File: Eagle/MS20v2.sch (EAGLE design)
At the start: 62 parts, among them IC1 LM13700M, IC2 TL074D, T1 2N3906, T2 2N3906

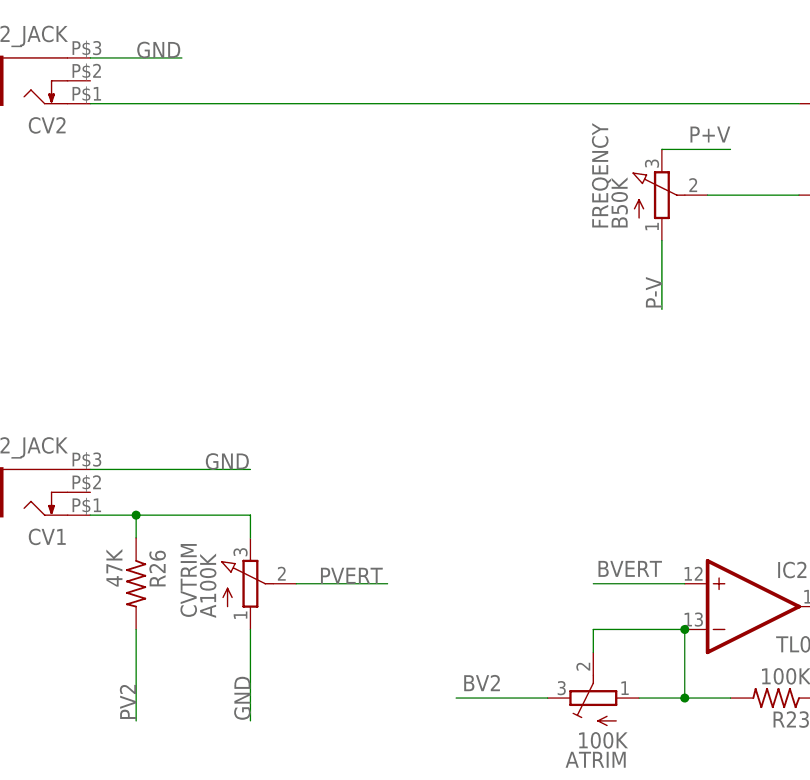
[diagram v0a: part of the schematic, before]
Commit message: updated Pot designations/values
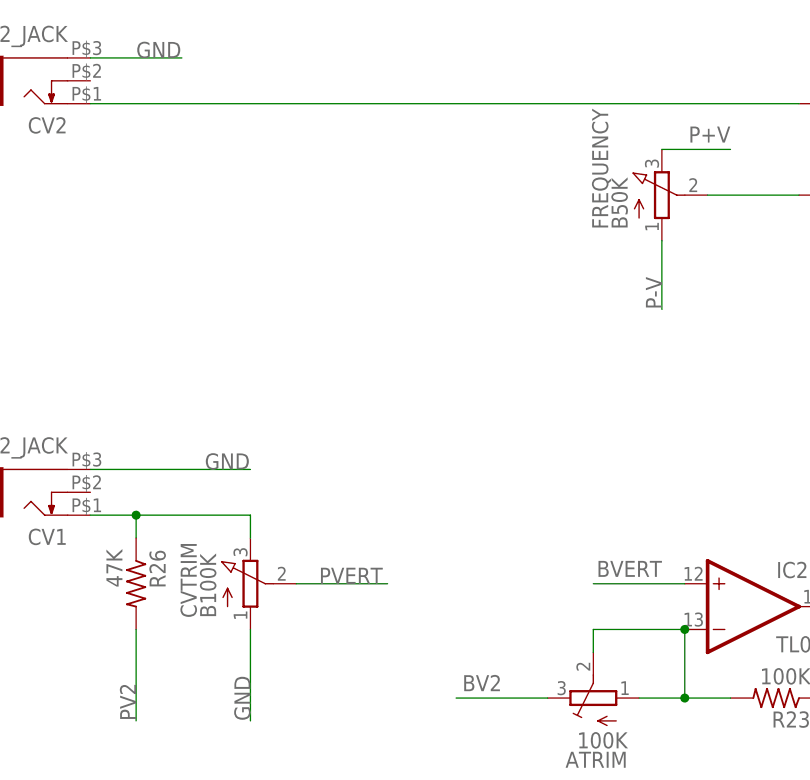
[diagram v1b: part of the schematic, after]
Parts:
- CVTRIM: value A100K -> B100K
- renumbered FREQENCY to FREQUENCY
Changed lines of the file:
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@@
 <part name="ATRIM" library="adafruit" deviceset="TRIMPOT" device="TC33X" value="100K"/>
 <part name="FTUNE" library="adafruit" deviceset="TRIMPOT" device="TC33X" value="1K"/>
-<part name="FREQENCY" library="pot" deviceset="EVU" device="A" technology="F2" value="B50K"/>
-<part name="CVTRIM" library="pot" deviceset="EVU" device="A" technology="F2" value="A100K"/>
+<part name="FREQUENCY" library="pot" deviceset="EVU" device="A" technology="F2" value="B50K"/>
+<part name="CVTRIM" library="pot" deviceset="EVU" device="A" technology="F2" value="B100K"/>
 <part name="INVOL" library="pot" deviceset="EVU" device="A" technology="F2" value="A100K"/>
 <part name="RESONANCE" library="pot" deviceset="EVU" device="A" technology="F2" value="A100K"/>
@@
 <attribute name="VALUE" x="57.15" y="135.89" size="1.778" layer="96" rot="R90"/>
 </instance>
-<instance part="FREQENCY" gate="G$1" x="-2.54" y="205.74" smashed="yes" grouprefs="4">
+<instance part="FREQUENCY" gate="G$1" x="-2.54" y="205.74" smashed="yes" grouprefs="4">
 <attribute name="NAME" x="-8.509" y="201.93" size="1.778" layer="95" rot="R90"/>
 <attribute name="VALUE" x="-6.35" y="201.93" size="1.778" layer="96" rot="R90"/>
@@
 <wire x1="58.42" y1="12.7" x2="63.5" y2="12.7" width="0.1524" layer="91"/>
 <pinref part="C4" gate="G$1" pin="1"/>
-<wire x1="63.5" y1="12.7" x2="63.5" y2="40.64" width="0.1524" layer="91" grouprefs="1"/>
+<wire x1="63.5" y1="12.7" x2="63.5" y2="40.64" width="0.1524" layer="91"/>
 <junction x="63.5" y="12.7"/>
 <pinref part="LED2" gate="G$1" pin="C"/>
@@
 <net name="N$40" class="0">
 <segment>
-<pinref part="FREQENCY" gate="G$1" pin="S"/>
+<pinref part="FREQUENCY" gate="G$1" pin="S"/>
 <pinref part="R25" gate="G$1" pin="2"/>
 <wire x1="2.54" y1="205.74" x2="12.7" y2="205.74" width="0.1524" layer="91" grouprefs="4"/>
@@
 <net name="P-V" class="0">
 <segment>
-<pinref part="FREQENCY" gate="G$1" pin="A"/>
+<pinref part="FREQUENCY" gate="G$1" pin="A"/>
 <wire x1="-2.54" y1="200.66" x2="-2.54" y2="193.04" width="0.1524" layer="91" grouprefs="4"/>
 <label x="-2.54" y="193.04" size="1.778" layer="95" rot="R90" grouprefs="4"/>
@@
 <net name="P+V" class="0">
 <segment>
-<pinref part="FREQENCY" gate="G$1" pin="E"/>
+<pinref part="FREQUENCY" gate="G$1" pin="E"/>
 <wire x1="-2.54" y1="210.82" x2="5.08" y2="210.82" width="0.1524" layer="91" grouprefs="4"/>
 <label x="5.08" y="213.36" size="1.778" layer="95" rot="R180" grouprefs="4"/>

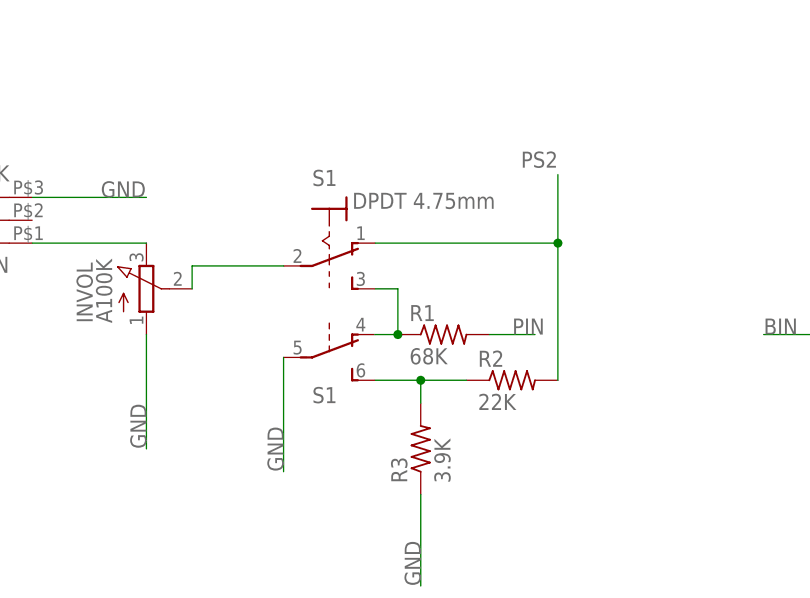
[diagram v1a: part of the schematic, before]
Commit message: changed HP/LP switch type to  TL46 P0
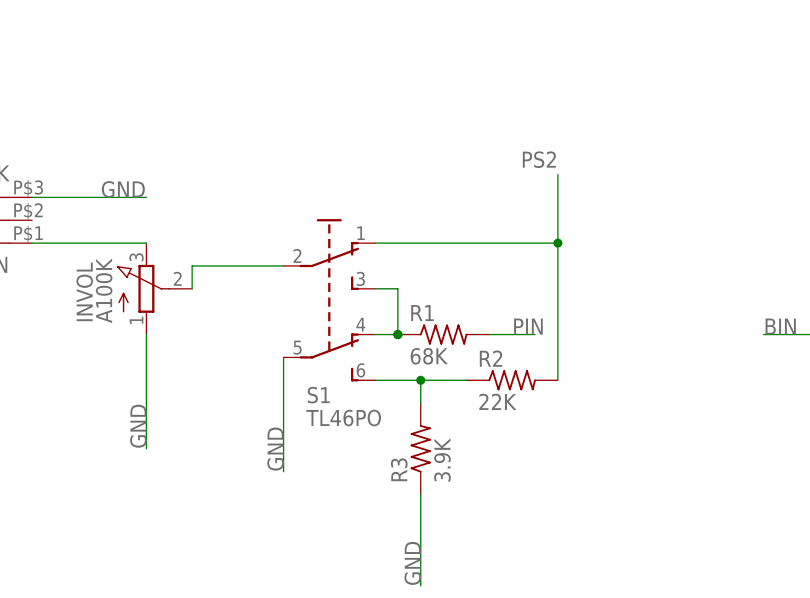
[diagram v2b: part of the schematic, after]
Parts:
- S1: value DPDT 4.75mm -> TL46PO; device switch:320-938 -> switch:TL46PO
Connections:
- net GND: now also S1.P1; no longer S1B.P
- net N$3: now also S1.O1, S1.S; no longer S11.S, S1B.O
- net N$30: now also S1.P; no longer S11.P
- net N$4: now also S1.S1; no longer S1B.S
- net PS2: now also S1.O; no longer S11.O
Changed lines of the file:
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@@
 <part name="D1" library="adafruit" library_urn="urn:adsk.eagle:library:420" deviceset="DIODE" device="SOD-123" package3d_urn="urn:adsk.eagle:package:6240753/1"/>
 <part name="D2" library="adafruit" library_urn="urn:adsk.eagle:library:420" deviceset="DIODE" device="SOD-123" package3d_urn="urn:adsk.eagle:package:6240753/1"/>
-<part name="S1" library="switch" library_urn="urn:adsk.eagle:library:380" deviceset="320-938" device="" package3d_urn="urn:adsk.eagle:package:27685/1" value="DPDT 4.75mm"/>
+<part name="S1" library="switch" library_urn="urn:adsk.eagle:library:380" deviceset="TL46PO" device="" package3d_urn="urn:adsk.eagle:package:27746/1"/>
 </parts>
 <sheets>
@@
 <attribute name="VALUE" x="214.63" y="205.74" size="1.27" layer="96" rot="R270"/>
 </instance>
-<instance part="S1" gate="B" x="-33.02" y="63.5" smashed="yes" rot="R270" grouprefs="6">
-<attribute name="PART" x="-34.925" y="58.42" size="1.778" layer="95"/>
-</instance>
-<instance part="S1" gate="1" x="-33.02" y="76.2" smashed="yes" rot="R270" grouprefs="6">
-<attribute name="VALUE" x="-30.48" y="80.01" size="1.778" layer="96"/>
-<attribute name="PART" x="-34.925" y="82.55" size="1.778" layer="95"/>
+<instance part="S1" gate="BEF1" x="-33.02" y="73.66" smashed="yes" rot="R270">
+<attribute name="NAME" x="-35.56" y="58.42" size="1.778" layer="95"/>
+<attribute name="VALUE" x="-35.56" y="55.88" size="1.778" layer="96"/>
 </instance>
 </instances>
@@
 <label x="-38.1" y="50.8" size="1.778" layer="95" rot="R90" grouprefs="6"/>
 <wire x1="-38.1" y1="63.5" x2="-38.1" y2="50.8" width="0.1524" layer="91" grouprefs="6"/>
-<pinref part="S1" gate="B" pin="P"/>
+<pinref part="S1" gate="BEF1" pin="P1"/>
 </segment>
 <segment>
@@
 <pinref part="R1" gate="G$1" pin="1"/>
 <wire x1="-27.94" y1="66.04" x2="-25.4" y2="66.04" width="0.1524" layer="91" grouprefs="6"/>
-<wire x1="-27.94" y1="71.12" x2="-25.4" y2="71.12" width="0.1524" layer="91" grouprefs="6"/>
-<wire x1="-25.4" y1="71.12" x2="-25.4" y2="66.04" width="0.1524" layer="91" grouprefs="6"/>
-<junction x="-25.4" y="66.04" grouprefs="6"/>
-<pinref part="S1" gate="B" pin="O"/>
-<pinref part="S1" gate="1" pin="S"/>
+<pinref part="S1" gate="BEF1" pin="O1"/>
+<pinref part="S1" gate="BEF1" pin="S"/>
+<wire x1="-27.94" y1="71.12" x2="-25.4" y2="71.12" width="0.1524" layer="91"/>
+<wire x1="-25.4" y1="71.12" x2="-25.4" y2="66.04" width="0.1524" layer="91"/>
+<junction x="-25.4" y="66.04"/>
 </segment>
 </net>
@@
 <wire x1="-22.86" y1="58.42" x2="-22.86" y2="60.96" width="0.1524" layer="91" grouprefs="6"/>
 <junction x="-22.86" y="60.96" grouprefs="6"/>
-<pinref part="S1" gate="B" pin="S"/>
+<pinref part="S1" gate="BEF1" pin="S1"/>
 </segment>
 </net>
@@
 <wire x1="-38.1" y1="73.66" x2="-48.26" y2="73.66" width="0.1524" layer="91" grouprefs="6"/>
 <wire x1="-48.26" y1="73.66" x2="-48.26" y2="71.12" width="0.1524" layer="91" grouprefs="6"/>
-<pinref part="S1" gate="1" pin="P"/>
+<pinref part="S1" gate="BEF1" pin="P"/>
 </segment>
 </net>
@@
 <wire x1="-7.62" y1="76.2" x2="-7.62" y2="83.82" width="0.1524" layer="91" grouprefs="6"/>
 <junction x="-7.62" y="76.2" grouprefs="6"/>
-<pinref part="S1" gate="1" pin="O"/>
+<pinref part="S1" gate="BEF1" pin="O"/>
 </segment>
 </net>
@@
 </segment>
 </net>
+<net name="N$24" class="0">
+<segment>
+<junction x="-25.4" y="66.04" grouprefs="6"/>
+</segment>
+</net>

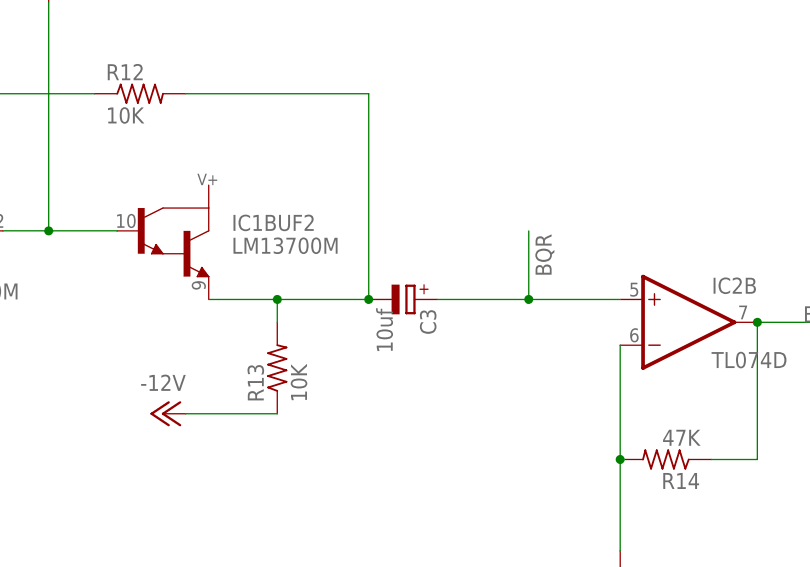
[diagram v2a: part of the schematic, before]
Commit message: Changed 10uf cap to 0,47uf cap
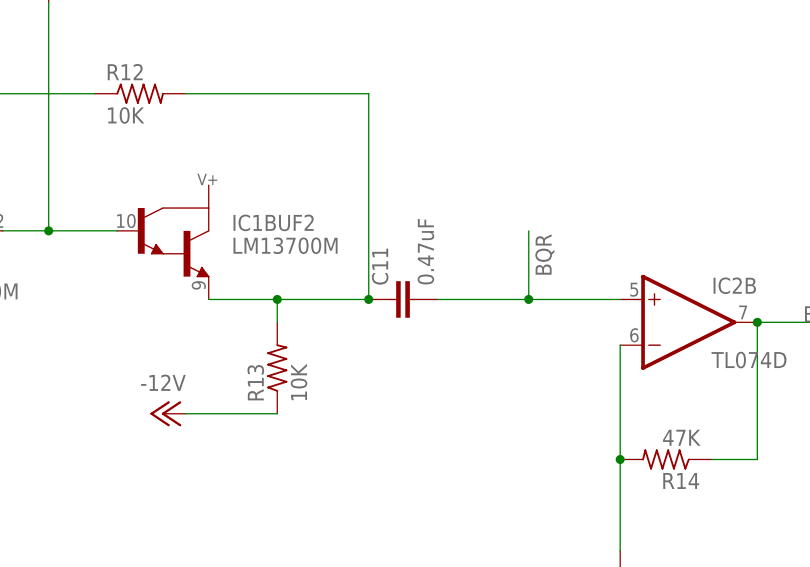
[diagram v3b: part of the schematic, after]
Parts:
- removed C3: 10uf, rcl:CPOL-EU153CLV-0405
- added C11: 0.47uF, rcl:C-EUC0603
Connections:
- net BQR: now also C11.2; no longer C3.+
- net N$16: now also C11.1; no longer C3.-
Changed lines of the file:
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@@
 <part name="C1" library="rcl" library_urn="urn:adsk.eagle:library:334" deviceset="CPOL-EU" device="153CLV-0405" package3d_urn="urn:adsk.eagle:package:23397/2" value="10uf"/>
 <part name="C2" library="rcl" library_urn="urn:adsk.eagle:library:334" deviceset="CPOL-EU" device="153CLV-0405" package3d_urn="urn:adsk.eagle:package:23397/2" value="10uf"/>
-<part name="C3" library="rcl" library_urn="urn:adsk.eagle:library:334" deviceset="CPOL-EU" device="153CLV-0405" package3d_urn="urn:adsk.eagle:package:23397/2" value="10uf"/>
 <part name="C4" library="rcl" deviceset="C-EU" device="C0603" value="1nF"/>
 <part name="C5" library="rcl" deviceset="C-EU" device="C0603" value="1nF"/>
@@
 <part name="D2" library="adafruit" library_urn="urn:adsk.eagle:library:420" deviceset="DIODE" device="SOD-123" package3d_urn="urn:adsk.eagle:package:6240753/1"/>
 <part name="S1" library="switch" library_urn="urn:adsk.eagle:library:380" deviceset="TL46PO" device="" package3d_urn="urn:adsk.eagle:package:27746/1"/>
+<part name="C11" library="rcl" deviceset="C-EU" device="C0603" value="0.47uF"/>
 </parts>
 <sheets>
@@
 <attribute name="VALUE" x="211.709" y="184.404" size="1.778" layer="96" rot="R270"/>
 </instance>
-<instance part="C3" gate="G$1" x="187.96" y="53.34" smashed="yes" rot="R270">
-<attribute name="NAME" x="188.595" y="52.324" size="1.778" layer="95" rot="R270"/>
-<attribute name="VALUE" x="183.769" y="52.324" size="1.778" layer="96" rot="R270"/>
-</instance>
 <instance part="C4" gate="G$1" x="63.5" y="43.18" smashed="yes" rot="R180">
 <attribute name="NAME" x="61.976" y="42.799" size="1.778" layer="95" rot="R270"/>
@@
 <attribute name="NAME" x="-35.56" y="58.42" size="1.778" layer="95"/>
 <attribute name="VALUE" x="-35.56" y="55.88" size="1.778" layer="96"/>
+</instance>
+<instance part="C11" gate="G$1" x="185.42" y="53.34" smashed="yes" rot="R90">
+<attribute name="NAME" x="185.039" y="54.864" size="1.778" layer="95" rot="R90"/>
+<attribute name="VALUE" x="190.119" y="54.864" size="1.778" layer="96" rot="R90"/>
 </instance>
 </instances>
@@
 <wire x1="172.72" y1="50.8" x2="172.72" y2="53.34" width="0.1524" layer="91"/>
 <junction x="172.72" y="53.34"/>
-<pinref part="C3" gate="G$1" pin="-"/>
+<pinref part="C11" gate="G$1" pin="1"/>
 <junction x="182.88" y="53.34"/>
 </segment>
@@
 <wire x1="210.82" y1="53.34" x2="200.66" y2="53.34" width="0.1524" layer="91"/>
 <label x="203.2" y="55.88" size="1.778" layer="95" rot="R90"/>
-<pinref part="C3" gate="G$1" pin="+"/>
 <wire x1="200.66" y1="53.34" x2="190.5" y2="53.34" width="0.1524" layer="91"/>
 <wire x1="200.66" y1="53.34" x2="200.66" y2="60.96" width="0.1524" layer="91"/>
 <junction x="200.66" y="53.34"/>
-</segment>
-</net>
+<pinref part="C11" gate="G$1" pin="2"/>
+</segment>
+</net>
